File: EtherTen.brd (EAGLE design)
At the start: 68.6 x 53.3 mm, 98 parts, among them IC1 MC33269DT-5.0, IC2 APX811-44UG-7, IC3 ATMEGA16U2-MU, IC4 LM358D, IC5 ATMEGA328P TQFP32, IC6 W5100SQFP80, J1 DC_2_1MM, P1 USB-6PSMT, P2 ICSP:MAIN, P3 ICSP:USB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

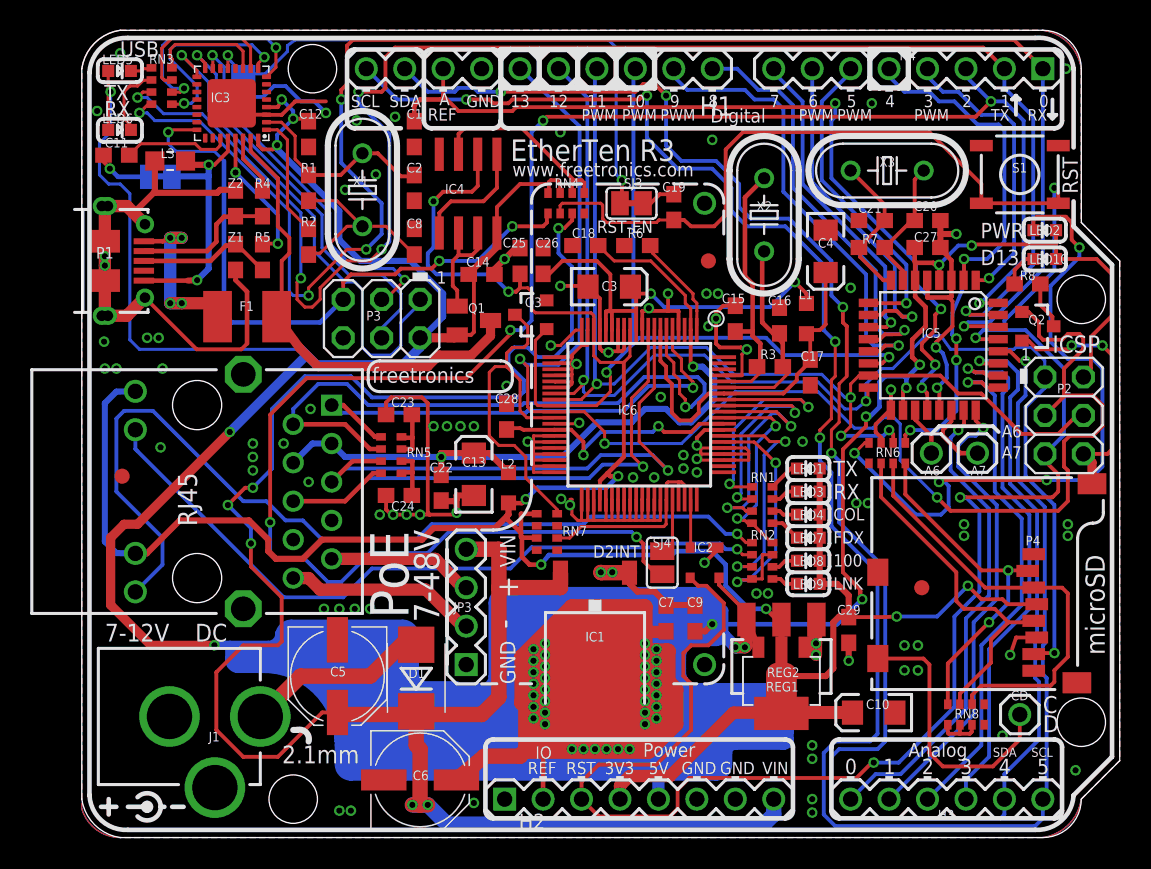
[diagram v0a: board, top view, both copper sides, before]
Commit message: Added I2C MAC ROM in preparation for v3.0
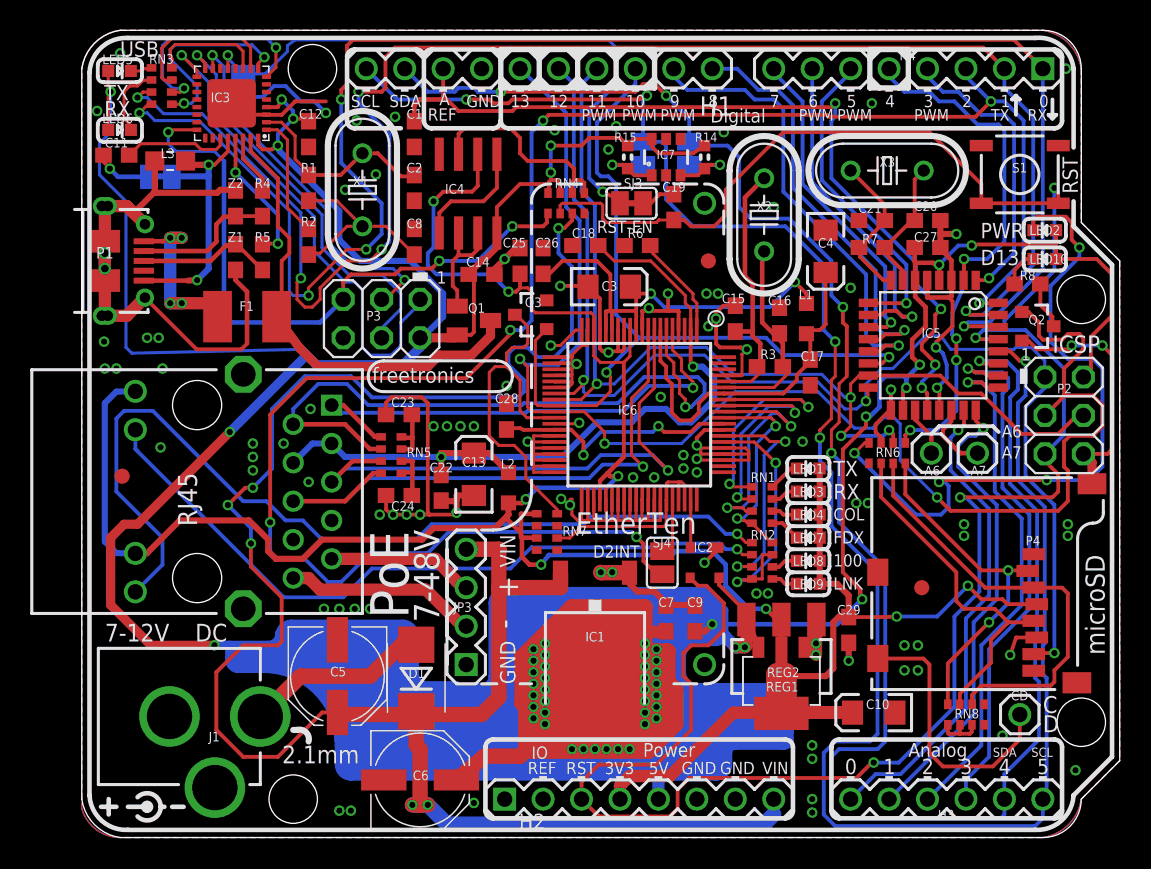
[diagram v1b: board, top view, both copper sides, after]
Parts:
- added IC7: MCP24AA025E48, freetronics-jon:SOT23-6
- added R14, R15: 4K7, freetronics-master-v1.1:0603
- added SJ5, SJ6: (no value), freetronics-jon:SJC
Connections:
- new net N$29: IC7.3, R14.2, SJ5.2
- new net N$5: IC7.1, R15.2, SJ6.2
- net 5V: now also IC7.6, R14.1, R15.1; no longer H2.2
- net A4_SDA: now also SJ5.1
- net A5_SCL: now also SJ6.1
- net GND: now also IC7.2, IC7.4, IC7.5
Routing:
- net 5V: track 1234.7 -> 1240.6 mm, vias 51 -> 53
- net N$5: track 0.00 -> 4.92 mm, vias 0 -> 1
- net N$29: track 0.00 -> 4.92 mm, vias 0 -> 1
- net D10_SS: track 51.9 -> 54.0 mm
- net DTR: track 39.0 -> 40.7 mm
- net A5_SCL: track 128.5 -> 130.2 mm
- net RESET: track 146.0 -> 144.4 mm
- net N$12: track 12.9 -> 13.9 mm
- net N$9: track 36.7 -> 37.7 mm
- net D11_MOSI: track 69.1 -> 70.0 mm
- net GND: vias 98 -> 101
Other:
- board text added: "ISOLATE"
- board text added: "MCP 24AA025E48 I2C ADDR: 70 (0x50)"
- board text added: "SDA/SCL"
- board text added: "SKU: ET"
- board text added: "by Marc Alexander and Jonathan Oxer"
- board text added: "v3.0"
- board text added: "www.freetronics.com/et"
- board text removed: "ETHERTEN"
- board text removed: "EtherTen R3"
- board text removed: "R3"
- board text removed: "SKU:"
- board text removed: "by Marc Alexander"
- board text removed: "v2.0"
- board text removed: "www.freetronics.com"
- board text removed: "www.freetronics.com/etherten"
